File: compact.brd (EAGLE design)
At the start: 21.6 x 57.1 mm, 38 parts, among them J3 AVX_6-PIN_009159006061916, J4 CORTEX_DEBUG_PTH, J5 10118194-0001LF, U1 STM32F103C8T6, U2 CJT1117-3.3-SOT223

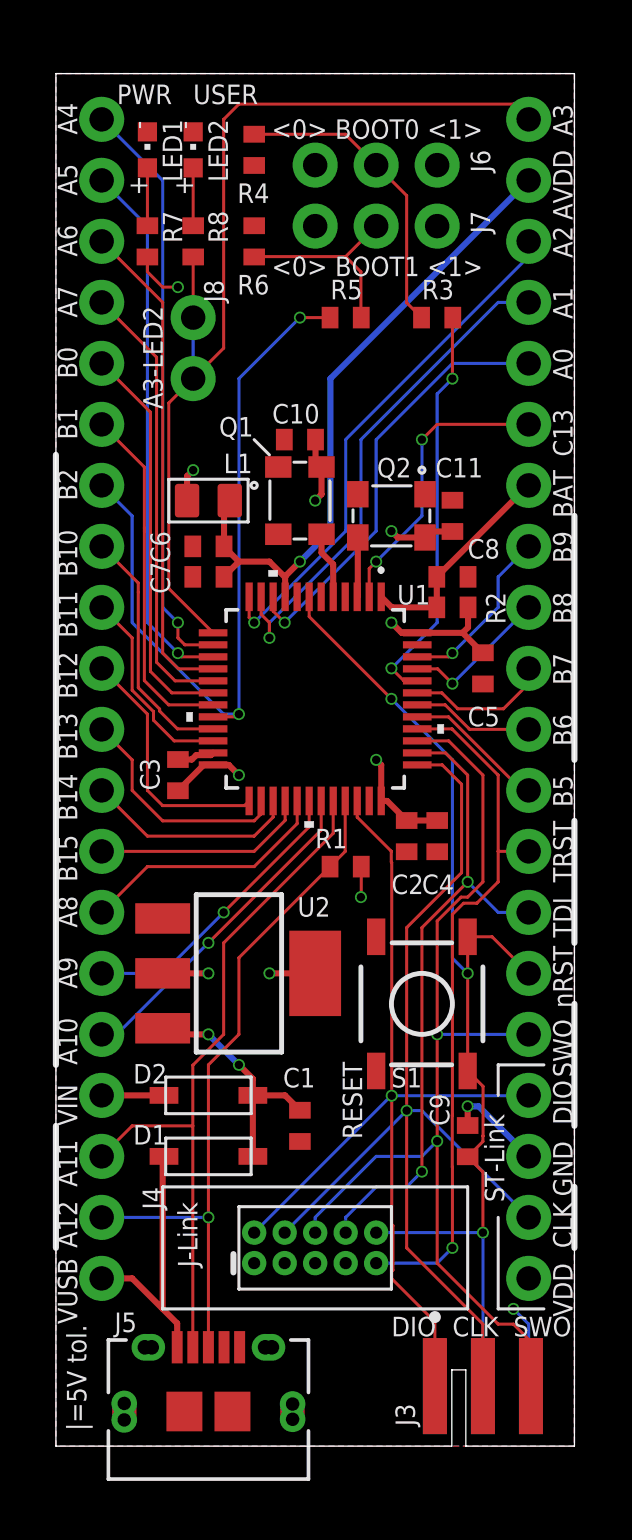
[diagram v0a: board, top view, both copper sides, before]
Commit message: Changed USB connector to mini-B. Change pin labels on the silkscreen to be more readable.
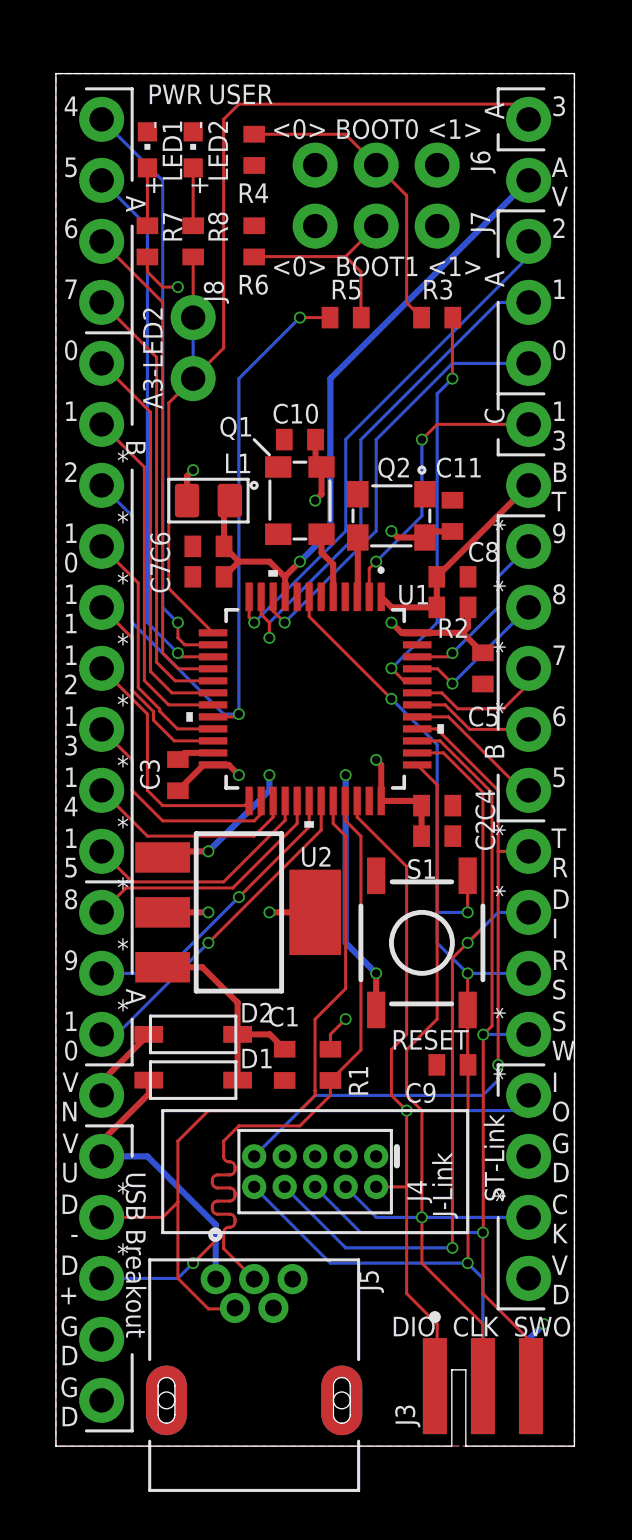
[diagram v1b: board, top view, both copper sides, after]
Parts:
- added J9: (no value), SparkFun-Connectors:1X11_NO_SILK
- J1: device SparkFun-Connectors:1X20_NOSILK -> SparkFun-Connectors:1X11_NO_SILK
- J5: value 10118194-0001LF -> 2172034-1; device USB-micro-B_Amphenol_10118194-0001LF:CONN_10118194-0001LF_AMP -> USB-mini-B_TE_2172034-1:TE_2172034-1
- moved R1 8.28 mm to (11.4, 15.9), turned to 90 degrees
- moved D1 3.24 mm to (5.71, 15.2)
- moved C9 3.24 mm to (16.5, 15.9), turned to 180 degrees
- moved J4 3.17 mm to (10.8, 11.4), turned to 180 degrees
- moved C1 2.62 mm to (9.53, 15.9)
- moved D2 2.62 mm to (5.71, 17.1)
- moved U2 2.54 mm to (7.62, 22.2)
- moved S1 2.54 mm to (15.2, 21.0)
- moved J5 1.94 mm to (8.26, 1.91), turned to 270 degrees
- moved C4 1.27 mm to (15.9, 26.7), turned to 0 degrees
- moved C2 1.27 mm to (15.9, 25.4), turned to 0 degrees
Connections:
- net GND: now also J5.SH1, J5.SH2, J9.10, J9.11; no longer J5.10, J5.11, J5.S_1, J5.S_1_H1, J5.S_1_H2, J5.S_2, J5.S_2_H1, J5.S_2_H2, J5.S_3, J5.S_3_H1, J5.S_3_H2, J5.S_4, J5.S_4_H1, J5.S_4_H2
- net PA10*: now also J9.5; no longer J1.16
- net PA8*: now also J9.3; no longer J1.14
- net PA9*: now also J9.4; no longer J1.15
- net PB14*: now also J9.1; no longer J1.12
- net PB15*: now also J9.2; no longer J1.13
- net USB_DM*: now also J9.8; no longer J1.18
- net USB_DP*: now also J9.9; no longer J1.19
- net VIN_4.8-15V: now also J9.6; no longer J1.17
- net VUSB: now also J9.7; no longer J1.20
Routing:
- net GND: track 9.30 -> 20.9 mm, vias 2 -> 5
- net SWCLK*: track 43.6 -> 36.2 mm
- net SWDIO*: track 39.5 -> 32.9 mm
- net JTDI*: track 27.4 -> 34.0 mm
- net NRST: track 45.5 -> 51.4 mm, vias 3 -> 4
- net USB_DP*: track 29.6 -> 33.6 mm
- net SWO*: track 42.5 -> 39.4 mm
- net USB_DM*: track 29.5 -> 31.6 mm
- net PB15*: track 8.98 -> 10.0 mm
- net VIN: track 10.1 -> 9.18 mm, vias 2 -> 0
- net VUSB: track 11.3 -> 12.2 mm
- net VIN_4.8-15V: track 2.59 -> 3.35 mm
- net VDD: track 27.2 -> 27.8 mm
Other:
- board text added: "*"
- board text added: "-------POWER------- VDD/AVDD: 2-3.6V. Must be 3.3V if C39- 097/C387- 415 are used for Q1/Q2. VUSB: 5V from USB (J5) VIN: 4.8-15V BAT: 1.8-3.6V. Short R2 if unused. ***WARNING***: Do NOT power MCU from VDD if EITHER VIN or USB (J5) are also being used. --------GPIO-------- Max current, ea pin: 25 mA Max current, total: 150 mA OUT (minus MCU power, ~7 -50 mA) and 150 mA IN (minus MCU po- wer) *=5V 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"
- board text added: "0"
- board text added: "1"
- board text added: "1 0"
- board text added: "1 1"
- board text added: "1 2"
- board text added: "1 3"
- board text added: "1 4"
- board text added: "1 5"
- board text added: "2"
- board text added: "3"
- board text added: "4"
- board text added: "5"
- board text added: "6"
- board text added: "7"
- board text added: "8"
- board text added: "9"
- board text added: "A"
- board text added: "A V"
- board text added: "B"
- board text added: "B T"
- board text added: "C"
- board text added: "C K"
- board text added: "D +"
- board text added: "D -"
- board text added: "D I"
- board text added: "G D"
- board text added: "I O"
- board text added: "R S"
- board text added: "S W"
- board text added: "T R"
- board text added: "USB Breakout"
- board text added: "V D"
- board text added: "V N"
- board text added: "V U"
- board text removed: "-------POWER------- VDD/AVDD: 2-3.6V. Must be 3.3V if C39- 097/C387- 415 are used for Q1/Q2. VUSB: 5V from USB (J5) VIN: 4.8-15V BAT: 1.8-3.6V. Short R2 if unused. ***WARNING***: Do NOT power MCU from VDD if EITHER VIN or USB (J5) are also being used. --------GPIO-------- Max current, ea pin: 25 mA Max current, total: 150 mA OUT (minus MCU power, ~7 -50 mA) and 150 mA IN (minus MCU po- wer) Bar o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"
- board text removed: "A0"
- board text removed: "A1"
- board text removed: "A10"
- board text removed: "A11"
- board text removed: "A12"
- board text removed: "A2"
- board text removed: "A3"
- board text removed: "A4"
- board text removed: "A5"
- board text removed: "A6"
- board text removed: "A7"
- board text removed: "A8"
- board text removed: "A9"
- board text removed: "AVDD"
- board text removed: "B0"
- board text removed: "B1"
- board text removed: "B10"
- board text removed: "B11"
- board text removed: "B12"
- board text removed: "B13"
- board text removed: "B14"
- board text removed: "B15"
- board text removed: "B2"
- board text removed: "B5"
- board text removed: "B6"
- board text removed: "B7"
- board text removed: "B8"
- board text removed: "B9"
- board text removed: "BAT"
- board text removed: "C13"
- board text removed: "TDI"
- board text removed: "TRST"
- board text removed: "VIN"
- board text removed: "VUSB"
- board text removed: "|=5V tol."
